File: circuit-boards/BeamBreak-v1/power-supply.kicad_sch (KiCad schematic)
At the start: 22 parts, among them Q1 SI2318CDS-T1-GE3, U1 ITS41k0S-ME-N, U2 LM3478MA

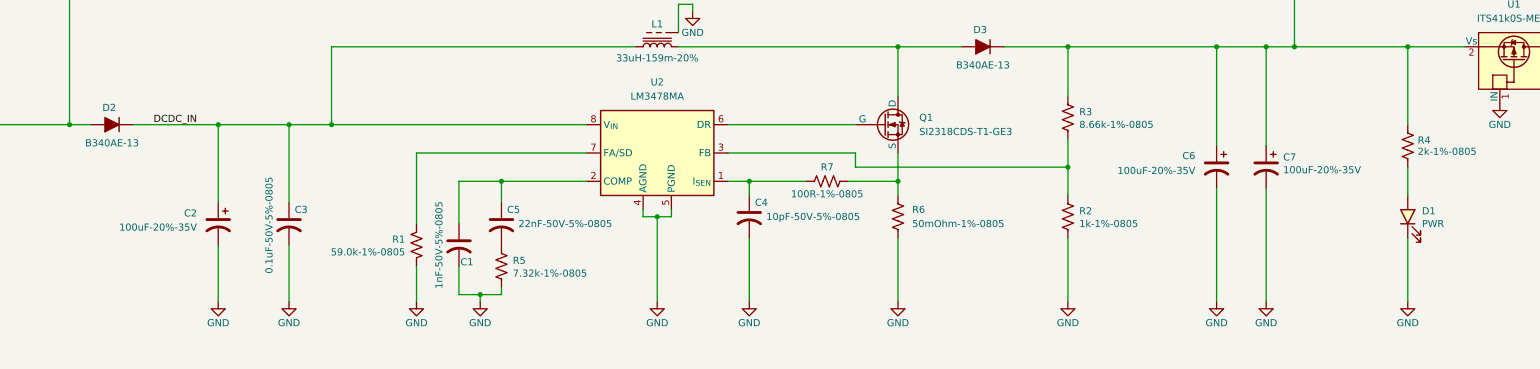
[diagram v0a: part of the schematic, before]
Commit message: Chagned opto-coupler to totem pole output to drive 5V DIO with weak pull-up
Signed-off-by: Scott Berman <sgberman1@gmail.com>
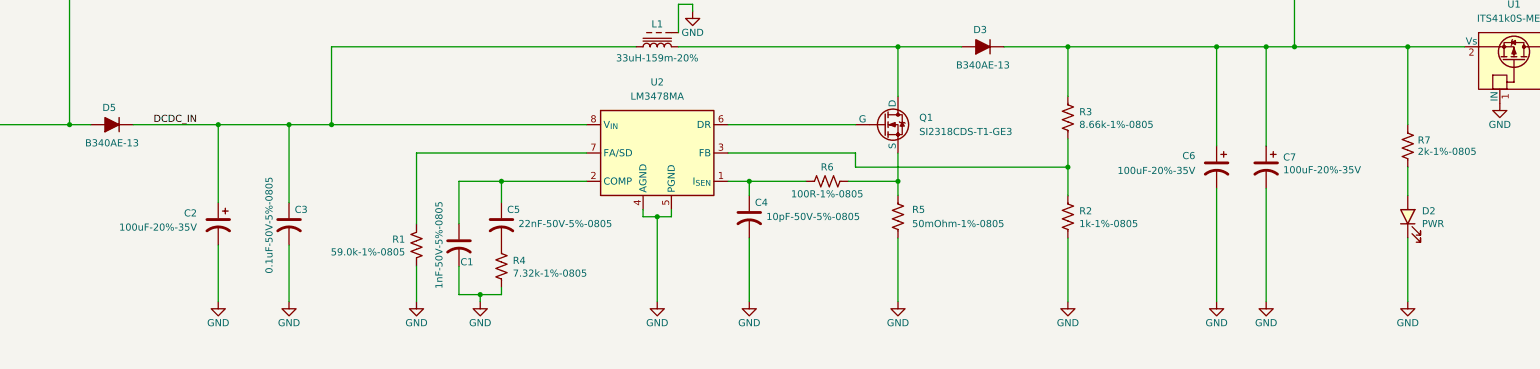
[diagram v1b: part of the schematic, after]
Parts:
- renumbered D1 to D2, D2 to D5, R5 to R4, R6 to R5, R7 to R6, R4 to R7
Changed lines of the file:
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@@
 	(title_block
 		(title "Beam Break Adapter")
-		(date "2026-01-02")
+		(date "2026-01-04")
 		(rev "1")
 		(company "1868 SPACE COOKIES")
@@
 		(on_board yes)
 		(dnp no)
-		(property "Reference" "D1"
+		(property "Reference" "D2"
 			(at 317.5 129.794 90)
 			(effects
@@
 			(project "BeamBreak-v1"
 				(path "/e06719a9-8757-4adc-9d1f-350085f61c1c/75796ea9-201f-4aa5-bea1-483188c429a4"
-					(reference "D1")
+					(reference "D2")
 					(unit 1)
 				)
@@
 		(dnp no)
 		(fields_autoplaced yes)
-		(property "Reference" "R6"
+		(property "Reference" "R5"
 			(at 226.06 129.5399 0)
 			(effects
@@
 			(project "BeamBreak-v1"
 				(path "/e06719a9-8757-4adc-9d1f-350085f61c1c/75796ea9-201f-4aa5-bea1-483188c429a4"
-					(reference "R6")
+					(reference "R5")
 					(unit 1)
 				)
@@
 		(on_board yes)
 		(dnp no)
-		(property "Reference" "R7"
+		(property "Reference" "R6"
 			(at 210.82 121.92 90)
 			(effects
@@
 			(project "BeamBreak-v1"
 				(path "/e06719a9-8757-4adc-9d1f-350085f61c1c/75796ea9-201f-4aa5-bea1-483188c429a4"
-					(reference "R7")
+					(reference "R6")
 					(unit 1)
 				)
@@
 		(on_board yes)
 		(dnp no)
-		(property "Reference" "D2"
+		(property "Reference" "D5"
 			(at 82.042 111.252 0)
 			(effects
@@
 			(project "BeamBreak-v1"
 				(path "/e06719a9-8757-4adc-9d1f-350085f61c1c/75796ea9-201f-4aa5-bea1-483188c429a4"
-					(reference "D2")
+					(reference "D5")
 					(unit 1)
 				)
@@
 		(on_board yes)
 		(dnp no)
-		(property "Reference" "R5"
+		(property "Reference" "R4"
 			(at 154.432 138.684 0)
 			(effects
@@
 			(project "BeamBreak-v1"
 				(path "/e06719a9-8757-4adc-9d1f-350085f61c1c/75796ea9-201f-4aa5-bea1-483188c429a4"
-					(reference "R5")
+					(reference "R4")
 					(unit 1)
 				)
@@
 		(on_board yes)
 		(dnp no)
-		(property "Reference" "R4"
+		(property "Reference" "R7"
 			(at 316.738 117.094 0)
 			(effects
@@
 			(project "BeamBreak-v1"
 				(path "/e06719a9-8757-4adc-9d1f-350085f61c1c/75796ea9-201f-4aa5-bea1-483188c429a4"
-					(reference "R4")
+					(reference "R7")
 					(unit 1)
 				)

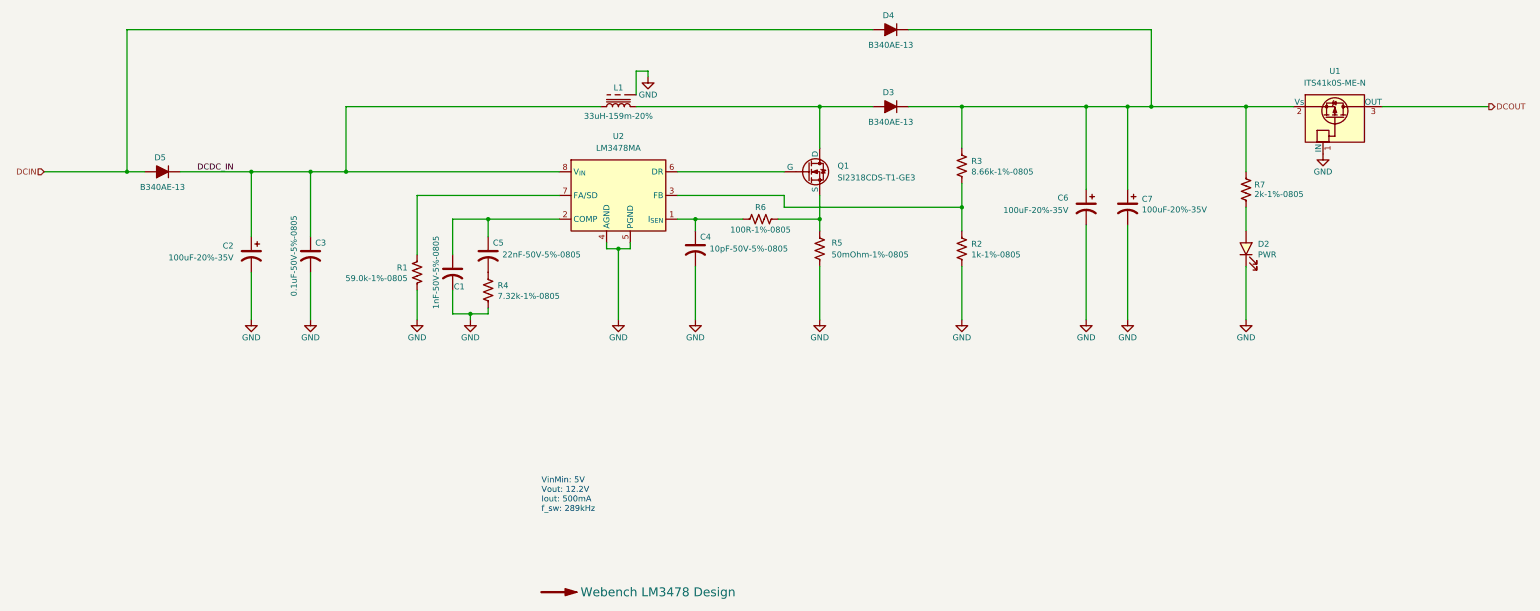
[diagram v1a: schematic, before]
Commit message: Improved placement and routing
Signed-off-by: Scott Berman <sgberman1@gmail.com>
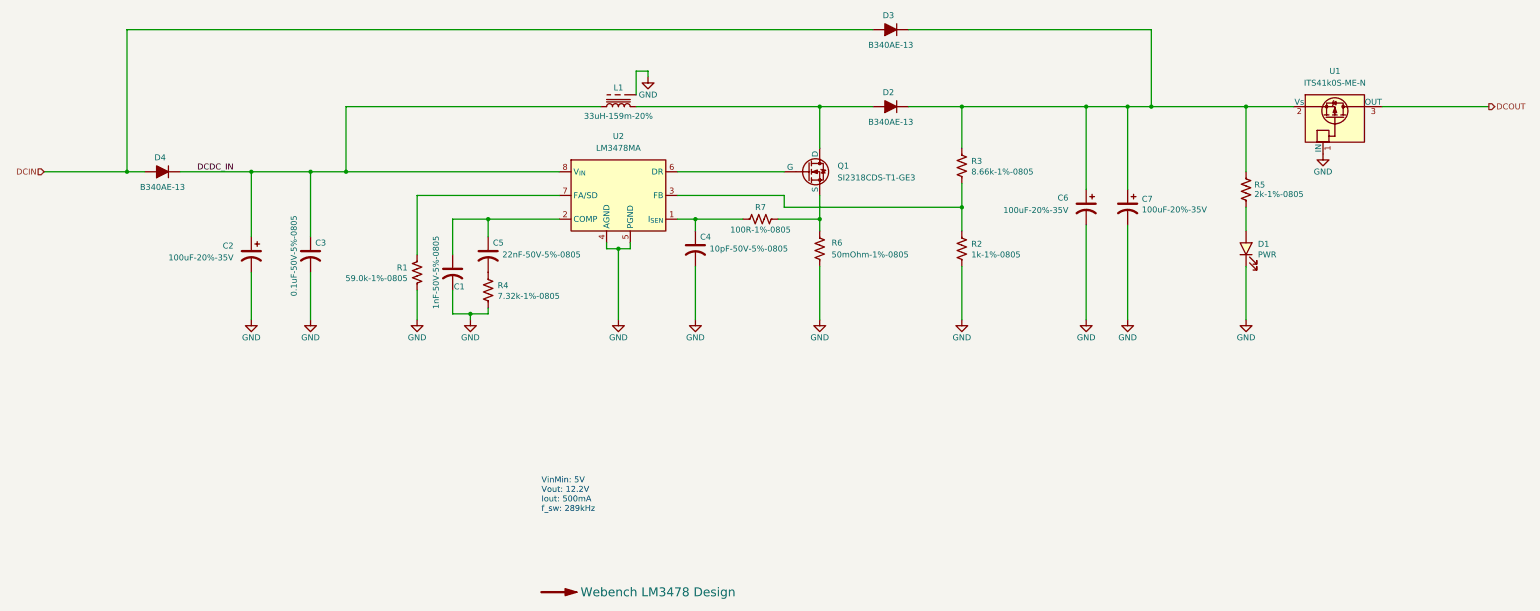
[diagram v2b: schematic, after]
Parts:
- renumbered D2 to D1, D3 to D2, D4 to D3, D5 to D4, R7 to R5, R5 to R6, R6 to R7
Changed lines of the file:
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@@
 		(on_board yes)
 		(dnp no)
-		(property "Reference" "D2"
+		(property "Reference" "D1"
 			(at 317.5 129.794 90)
 			(effects
@@
 			(project "BeamBreak-v1"
 				(path "/e06719a9-8757-4adc-9d1f-350085f61c1c/75796ea9-201f-4aa5-bea1-483188c429a4"
-					(reference "D2")
+					(reference "D1")
 					(unit 1)
 				)
@@
 		(dnp no)
 		(fields_autoplaced yes)
-		(property "Reference" "R5"
+		(property "Reference" "R6"
 			(at 226.06 129.5399 0)
 			(effects
@@
 			(project "BeamBreak-v1"
 				(path "/e06719a9-8757-4adc-9d1f-350085f61c1c/75796ea9-201f-4aa5-bea1-483188c429a4"
-					(reference "R5")
+					(reference "R6")
 					(unit 1)
 				)
@@
 		(on_board yes)
 		(dnp no)
-		(property "Reference" "D3"
+		(property "Reference" "D2"
 			(at 238.252 97.282 0)
 			(effects
@@
 			(project "BeamBreak-v1"
 				(path "/e06719a9-8757-4adc-9d1f-350085f61c1c/75796ea9-201f-4aa5-bea1-483188c429a4"
-					(reference "D3")
+					(reference "D2")
 					(unit 1)
 				)
@@
 		(on_board yes)
 		(dnp no)
-		(property "Reference" "R6"
+		(property "Reference" "R7"
 			(at 210.82 121.92 90)
 			(effects
@@
 			(project "BeamBreak-v1"
 				(path "/e06719a9-8757-4adc-9d1f-350085f61c1c/75796ea9-201f-4aa5-bea1-483188c429a4"
-					(reference "R6")
+					(reference "R7")
 					(unit 1)
 				)
@@
 		(on_board yes)
 		(dnp no)
-		(property "Reference" "D5"
+		(property "Reference" "D4"
 			(at 82.042 111.252 0)
 			(effects
@@
 			(project "BeamBreak-v1"
 				(path "/e06719a9-8757-4adc-9d1f-350085f61c1c/75796ea9-201f-4aa5-bea1-483188c429a4"
-					(reference "D5")
+					(reference "D4")
 					(unit 1)
 				)
@@
 		(on_board yes)
 		(dnp no)
-		(property "Reference" "R7"
+		(property "Reference" "R5"
 			(at 316.738 117.094 0)
 			(effects
@@
 			(project "BeamBreak-v1"
 				(path "/e06719a9-8757-4adc-9d1f-350085f61c1c/75796ea9-201f-4aa5-bea1-483188c429a4"
-					(reference "R7")
+					(reference "R5")
 					(unit 1)
 				)
@@
 		(on_board yes)
 		(dnp no)
-		(property "Reference" "D4"
+		(property "Reference" "D3"
 			(at 238.252 80.772 0)
 			(effects
@@
 			(project "BeamBreak-v1"
 				(path "/e06719a9-8757-4adc-9d1f-350085f61c1c/75796ea9-201f-4aa5-bea1-483188c429a4"
-					(reference "D4")
+					(reference "D3")
 					(unit 1)
 				)

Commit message: Fix inductor mfg part number
Signed-off-by: Scott Berman <sgberman1@gmail.com>
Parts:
- L1: DIST P/N 541-IHLE5050FHER6R8M5ACT-ND -> 541-IHLE3232DDER330M5ACT-ND; MFG P/N IHLE5050FHER6R8M5A -> IHLE3232DDER330M5A
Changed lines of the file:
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@@
 	(title_block
 		(title "Beam Break Adapter")
-		(date "2026-01-04")
+		(date "2026-02-22")
 		(rev "1")
 		(company "1868 SPACE COOKIES")
@@
 			)
 		)
-		(property "MFG P/N" "IHLE5050FHER6R8M5A"
+		(property "MFG P/N" "IHLE3232DDER330M5A"
 			(at 180.34 100.33 90)
 			(effects
@@
 			)
 		)
-		(property "DIST P/N" "541-IHLE5050FHER6R8M5ACT-ND"
+		(property "DIST P/N" "541-IHLE3232DDER330M5ACT-ND"
 			(at 180.34 100.33 90)
 			(effects
